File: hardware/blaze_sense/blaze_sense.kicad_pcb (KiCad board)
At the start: 2 copper layers, 70 x 70 mm, 2 parts, among them J2 Conn_01x30_Pin, J3 Conn_01x30_Socket

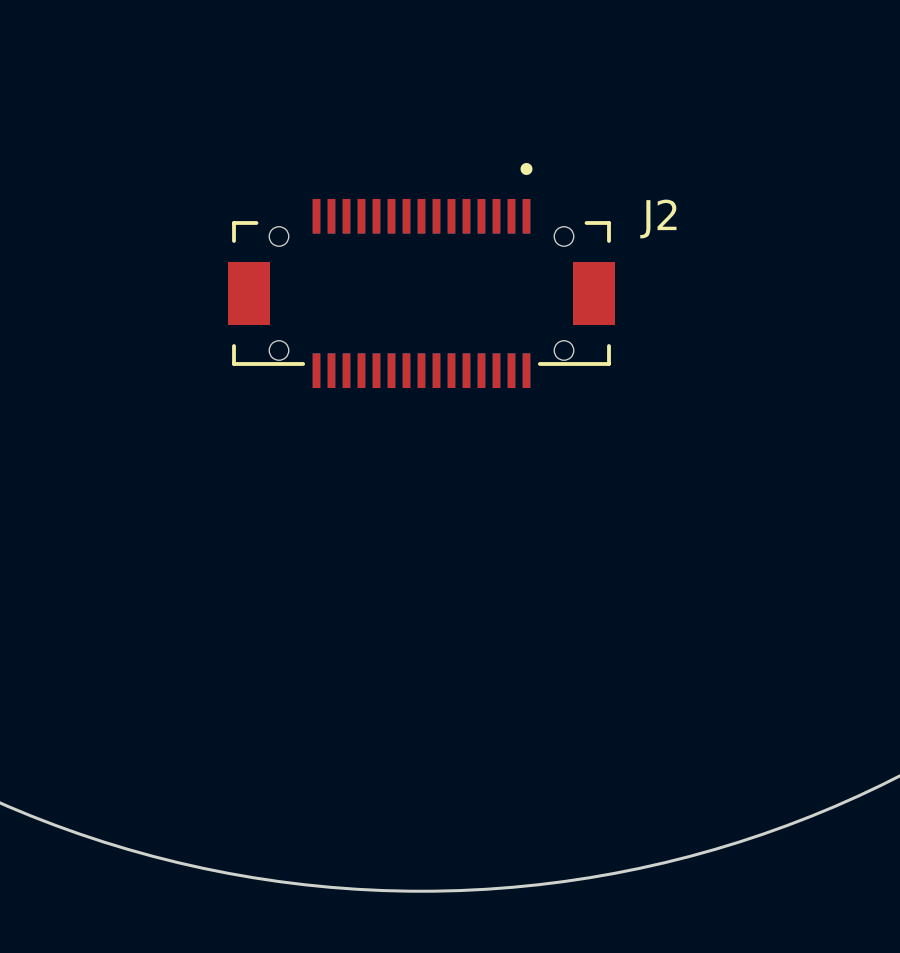
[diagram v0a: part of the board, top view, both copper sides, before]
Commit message: Brought in template PCB
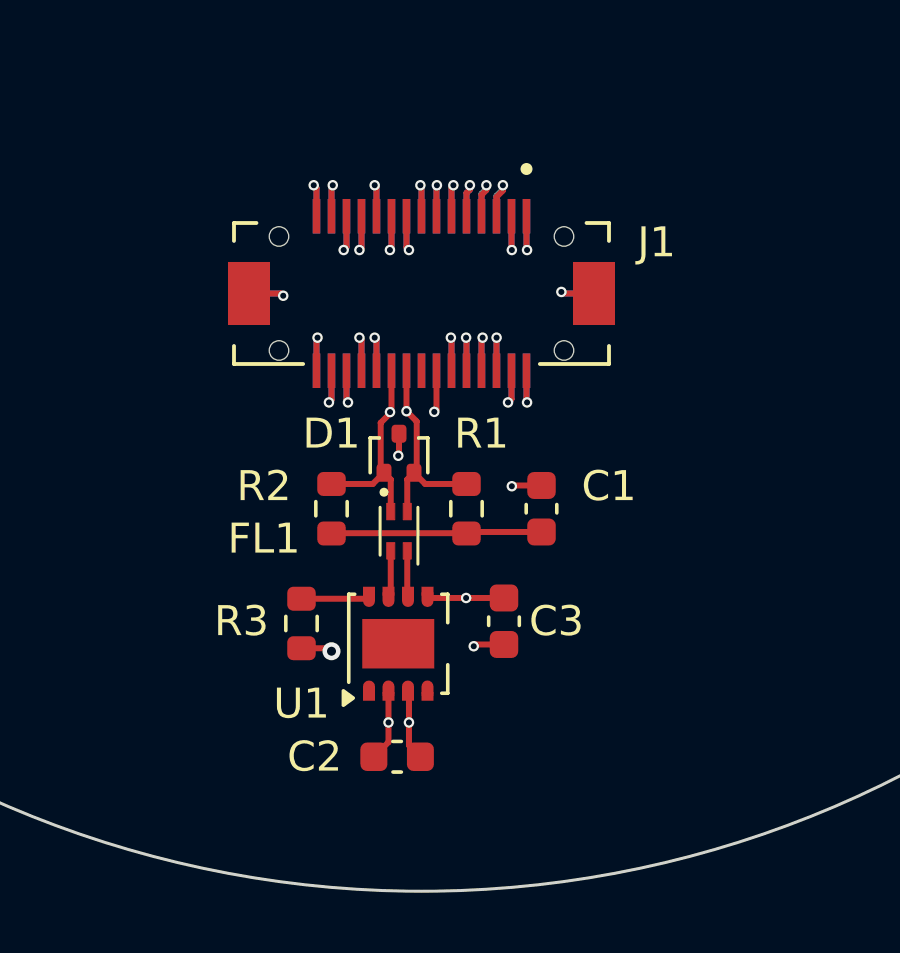
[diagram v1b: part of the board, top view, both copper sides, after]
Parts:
- added C1: 4.7nF, Capacitor_SMD:C_0603_1608Metric, F.Cu at (152.5, 127.8)
- added C2: 0.1uF, Capacitor_SMD:C_0603_1608Metric, F.Cu at (147.7, 136.0)
- added C3: 0.1uF, Capacitor_SMD:C_0603_1608Metric, F.Cu at (151.2, 131.5)
- added D1: ESDCAN03-2BM3Y, Package_TO_SOT_SMD:SOT-416, F.Cu at (147.8, 125.9)
- added FL1: Choke, Inductor_SMD:L_CommonModeChoke_Coilcraft_0603USB, F.Cu at (147.8, 128.5)
- added R1: 60, Resistor_SMD:R_0603_1608Metric, F.Cu at (150.0, 127.8)
- added R2: 60, Resistor_SMD:R_0603_1608Metric, F.Cu at (145.5, 127.8)
- added R3: 10K, Resistor_SMD:R_0603_1608Metric, F.Cu at (144.5, 131.6)
- added U1: TCAN1044VDDFR, Package_SON:Texas_S-PVSON-N8, F.Cu at (147.7, 132.2)
- J1: renamed from J2; value Conn_01x30_Pin -> FrontInterconnect
- J2: renamed from J3; value Conn_01x30_Socket -> RearInterconnect
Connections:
- J1 pad 1: Net-(J2-Pin_1) -> GND
- J1 pad 10: Net-(J2-Pin_10) -> +3V3
- J1 pad 11: +5V -> /PPS
- J1 pad 12: +3V3 -> GND
- J1 pad 13: /PPS -> GND
- J1 pad 14: GND -> Net-(J1-Pin_14)
- J1 pad 15: GND -> Net-(J1-Pin_15)
- J1 pad 16: Net-(J2-Pin_16) -> +3V3
- J1 pad 18: +3V3 -> Net-(J1-Pin_18)
- J1 pad 19: Net-(J2-Pin_19) -> GND
- J1 pad 2: Net-(J2-Pin_2) -> GND
- J1 pad 20: Net-(J2-Pin_20) -> GND
- J1 pad 21: GND -> /CANH
- J1 pad 22: GND -> /CANL
- J1 pad 23: /CANL -> Net-(J1-Pin_23)
- J1 pad 24: /CANH -> Net-(J1-Pin_24)
- J1 pad 25: Net-(J2-Pin_25) -> +5V
- J1 pad 26: Net-(J2-Pin_26) -> +5V
- J1 pad 27: +5V -> +3V3
- J1 pad 28: +5V -> +3V3
- J1 pad 29: +3V3 -> Net-(J1-Pin_29)
- J1 pad 3: GND -> /TX_RADIO
- J1 pad 30: +3V3 -> Net-(J1-Pin_30)
- J1 pad 4: GND -> /RX_RADIO
- J1 pad 5: /TX_RADIO -> Net-(J1-Pin_5)
- J1 pad 6: /RX_RADIO -> /ARM
- J1 pad 8: /ARM -> Net-(J1-Pin_8)
- J1 pad 9: Net-(J2-Pin_9) -> +5V
- J1 pad S1: (no net) -> GND
- J1 pad S2: (no net) -> GND
- J2 pad 1: +3V3 -> Net-(J1-Pin_30)
- J2 pad 10: GND -> /CANH
- J2 pad 11: Net-(J2-Pin_20) -> GND
- J2 pad 12: Net-(J2-Pin_19) -> GND
- J2 pad 13: +3V3 -> Net-(J1-Pin_18)
- J2 pad 15: Net-(J2-Pin_16) -> +3V3
- J2 pad 16: GND -> Net-(J1-Pin_15)
- J2 pad 17: GND -> Net-(J1-Pin_14)
- J2 pad 18: /PPS -> GND
- J2 pad 19: +3V3 -> GND
- J2 pad 2: +3V3 -> Net-(J1-Pin_29)
- J2 pad 20: +5V -> /PPS
- J2 pad 21: Net-(J2-Pin_10) -> +3V3
- J2 pad 22: Net-(J2-Pin_9) -> +5V
- J2 pad 23: /ARM -> Net-(J1-Pin_8)
- J2 pad 25: /RX_RADIO -> /ARM
- J2 pad 26: /TX_RADIO -> Net-(J1-Pin_5)
- J2 pad 27: GND -> /RX_RADIO
- J2 pad 28: GND -> /TX_RADIO
- J2 pad 29: Net-(J2-Pin_2) -> GND
- J2 pad 3: +5V -> +3V3
- J2 pad 30: Net-(J2-Pin_1) -> GND
- J2 pad 4: +5V -> +3V3
- J2 pad 5: Net-(J2-Pin_26) -> +5V
- J2 pad 6: Net-(J2-Pin_25) -> +5V
- J2 pad 7: /CANH -> Net-(J1-Pin_24)
- J2 pad 8: /CANL -> Net-(J1-Pin_23)
- J2 pad 9: GND -> /CANL
- J2 pad S1: (no net) -> GND
- J2 pad S2: (no net) -> GND
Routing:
- net +5V: track 0.00 -> 26.6 mm, vias 0 -> 4
- net GND: track 0.00 -> 23.2 mm, vias 0 -> 12
- net +3V3: track 0.00 -> 12.6 mm, vias 0 -> 6
- net Net-(C1-Pad1): track 0.00 -> 7.28 mm
- net /CANH: track 0.00 -> 6.94 mm, vias 0 -> 1
- net /CANL: track 0.00 -> 6.90 mm, vias 0 -> 1
- net /CAN_STB: track 0.00 -> 2.27 mm
- net /TX_RADIO: track 0.00 -> 2.24 mm, vias 0 -> 1
- net Net-(J1-Pin_29): track 0.00 -> 2.21 mm, vias 0 -> 1
- net /RX_RADIO: track 0.00 -> 2.20 mm, vias 0 -> 1
- net Net-(J1-Pin_17): track 0.00 -> 2.18 mm, vias 0 -> 1
- net Net-(J1-Pin_5): track 0.00 -> 2.16 mm, vias 0 -> 1
- net Net-(J1-Pin_18): track 0.00 -> 2.15 mm, vias 0 -> 1
- net Net-(J1-Pin_15): track 0.00 -> 2.14 mm, vias 0 -> 1
- net Net-(J1-Pin_30): track 0.00 -> 2.13 mm, vias 0 -> 1
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- added copper zone on In1.Cu, net +3V3
- added copper zone on In2.Cu, net GND
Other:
- copper layers 2 -> 4

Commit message: draft for julian to look over
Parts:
- added C1: 0.1uF, Capacitor_SMD:C_0603_1608Metric, F.Cu at (119.8, 103.9)
- added C10: 0.1uF, Capacitor_SMD:C_0603_1608Metric, F.Cu at (64.6, 82.8)
- added C11: 1uF, Capacitor_SMD:C_0603_1608Metric, F.Cu at (64.6, 85.3)
- added C12: 0.1uF, Capacitor_SMD:C_0603_1608Metric, F.Cu at (68.6, 60.2)
- added C13: 10nF, Capacitor_SMD:C_0603_1608Metric, F.Cu at (133.0, 88.2)
- added C14: 0.1uF, Capacitor_SMD:C_0603_1608Metric, F.Cu at (119.0, 96.9)
- added C15: 0.1uF, Capacitor_SMD:C_0603_1608Metric, F.Cu at (119.0, 94.8)
- added C16: 1uF, Capacitor_SMD:C_0603_1608Metric, F.Cu at (129.4, 99.3)
- added C17: 0.1uF, Capacitor_SMD:C_0603_1608Metric, F.Cu at (129.4, 101.3)
- added C18: 10uF, Capacitor_SMD:C_0603_1608Metric, F.Cu at (138.4, 85.3)
- added C19: 0.1uF, Capacitor_SMD:C_0603_1608Metric, F.Cu at (140.4, 85.3)
- added C2: 1uF, Capacitor_SMD:C_0603_1608Metric, F.Cu at (64.6, 62.8)
- added C20: 470nF, Capacitor_SMD:C_0603_1608Metric, F.Cu at (135.8, 88.2)
- added C21: 12.5pF, Capacitor_SMD:C_0603_1608Metric, F.Cu at (162.8, 112.5)
- added C22: 12.5pF, Capacitor_SMD:C_0603_1608Metric, F.Cu at (162.8, 108.9)
- added C23: 18pF, Capacitor_SMD:C_0603_1608Metric, F.Cu at (162.8, 104.5)
- added C24: 1uF, Capacitor_SMD:C_0603_1608Metric, F.Cu at (134.2, 102.3)
- added C25: 0.1uF, Capacitor_SMD:C_0603_1608Metric, F.Cu at (134.2, 100.5)
- added C26: 0.1uF, Capacitor_SMD:C_0603_1608Metric, F.Cu at (123.8, 103.9)
- added C27: 18pF, Capacitor_SMD:C_0603_1608Metric, F.Cu at (162.8, 100.7)
- added C28: 10uF, Capacitor_SMD:C_0603_1608Metric, F.Cu at (150.9, 98.2)
- added C29: 0.1uF, Capacitor_SMD:C_0603_1608Metric, F.Cu at (153.0, 98.3)
- added C3: 0.1uF, Capacitor_SMD:C_0603_1608Metric, F.Cu at (64.6, 65.3)
- added C30: 4.7nF, Capacitor_SMD:C_0603_1608Metric, F.Cu at (135.4, 126.3)
- added C31: 0.1uF, Capacitor_SMD:C_0603_1608Metric, F.Cu at (146.6, 115.5)
- added C32: 0.1uF, Capacitor_SMD:C_0603_1608Metric, F.Cu at (137.4, 115.5)
- added C33: 2.2uF, Capacitor_SMD:C_0603_1608Metric, F.Cu at (144.6, 97.8)
- added C34: 2.2uF, Capacitor_SMD:C_0603_1608Metric, F.Cu at (154.1, 114.3)
- added C35: 0.1uF, Capacitor_SMD:C_0603_1608Metric, F.Cu at (76.6, 62.8)
- added C36: 0.1uF, Capacitor_SMD:C_0603_1608Metric, F.Cu at (76.6, 65.3)
- added C37: 0.1uF, Capacitor_SMD:C_0603_1608Metric, F.Cu at (76.6, 67.8)
- added C38: 0.1uF, Capacitor_SMD:C_0603_1608Metric, F.Cu at (36.7, 64.8)
- added C39: 0.1uF, Capacitor_SMD:C_0603_1608Metric, F.Cu at (76.6, 72.8)
- added C4: 0.1uF, Capacitor_SMD:C_0603_1608Metric, F.Cu at (64.6, 67.8)
- added C40: 1uF, Capacitor_SMD:C_0603_1608Metric, F.Cu at (76.6, 75.3)
- added C5: 0.1uF, Capacitor_SMD:C_0603_1608Metric, F.Cu at (64.6, 70.3)
- added C6: 4.7uF, Capacitor_SMD:C_0603_1608Metric, F.Cu at (64.6, 72.8)
- added C7: 0.1uF, Capacitor_SMD:C_0603_1608Metric, F.Cu at (64.6, 75.3)
- added C8: 0.1uF, Capacitor_SMD:C_0603_1608Metric, F.Cu at (64.6, 77.8)
- added C9: 1uF, Capacitor_SMD:C_0603_1608Metric, F.Cu at (64.6, 80.3)
- added D1: D_Schottky, Diode_SMD:D_0603_1608Metric, F.Cu at (119.8, 106.3)
- added D2: ESDCAN03-2BM3Y, Package_TO_SOT_SMD:SOT-416, F.Cu at (142.3, 125.8)
- added FL1: Choke, Inductor_SMD:L_CommonModeChoke_Coilcraft_0603USB, F.Cu at (140.2, 121.4)
- added J2: Conn_01x30_Pin, BlazeLibrary:HRS_DF17_1.0H_-30DP-0.5V_57_, F.Cu at (173.3, 108.5)
- added J3: Conn_01x30_Socket, BlazeLibrary:HRS_DF17_1.0H_-30DP-0.5V_57_, F.Cu at (173.4, 100.3)
- added L1: L_Small, BlazeLibrary:SENSOR-XY-F-RM3100, F.Cu at (142.8, 82.8)
- added L2: L_Small, BlazeLibrary:SENSOR-XY-F-RM3100, F.Cu at (153.7, 85.3)
- added L3: L_Small, BlazeLibrary:SENSOR-Z-F-RM3100, F.Cu at (158.6, 94.9)
- added P1: TC2030-CTX, BlazeLibrary:TC2030-IDC-FP, F.Cu at (133.7, 108.0)
- added R10: 60, Resistor_SMD:R_0603_1608Metric, F.Cu at (138.3, 125.2)
- added R11: 60, Resistor_SMD:R_0603_1608Metric, F.Cu at (138.3, 127.3)
- added R12: 10K, Resistor_SMD:R_0603_1608Metric, F.Cu at (141.0, 130.6)
- added R2: 10k, Resistor_SMD:R_0603_1608Metric, F.Cu at (135.8, 84.5)
- added R3: 121, Resistor_SMD:R_0603_1608Metric, F.Cu at (148.3, 87.0)
- added R4: 121, Resistor_SMD:R_0603_1608Metric, F.Cu at (145.6, 87.0)
- added R5: 121, Resistor_SMD:R_0603_1608Metric, F.Cu at (154.8, 89.4)
- added R6: 121, Resistor_SMD:R_0603_1608Metric, F.Cu at (150.8, 89.4)
- added R7: 121, Resistor_SMD:R_0603_1608Metric, F.Cu at (153.1, 95.4)
- added R8: 121, Resistor_SMD:R_0603_1608Metric, F.Cu at (153.1, 93.0)
- added R9: 33k, Resistor_SMD:R_0603_1608Metric, F.Cu at (142.5, 88.2)
- added SW1: SW_SPST, Button_Switch_SMD:SW_SPST_B3U-1000P, F.Cu at (125.0, 108.0)
- added SW2: SW_SPDT, Button_Switch_SMD:Nidec_Copal_CAS-120A, F.Cu at (162.1, 124.5)
- added U1: ADXL375, BlazeLibrary:ADXL375BCCZ-RL, F.Cu at (132.0, 95.6)
- added U2: BMI088, BlazeLibrary:BMI088, F.Cu at (125.5, 94.9)
- added U3: A3G4250D, BlazeLibrary:A3G4250D, F.Cu at (139.5, 92.4)
- added U4: ADXL345, BlazeLibrary:ADXL345, F.Cu at (139.2, 99.1)
- added U5: MS5611-01BA, Package_LGA:LGA-8_3x5mm_P1.25mm, F.Cu at (124.7, 100.5)
- added U6: RM3100, BlazeLibrary:RM3100-13156, F.Cu at (146.6, 92.0)
- added U8: TCAN1044VDDFR, Package_SON:Texas_VSON-HR-8_1.5x2mm_P0.5mm, F.Cu at (142.0, 115.2)
- added U9: STM32H523RET6, BlazeLibrary:LQFP64_STM, F.Cu at (147.4, 107.0)
- added Y1: ABM3-8.000MHZ-B4Y-T, Crystal:Crystal_SMD_3215-2Pin_3.2x1.5mm, F.Cu at (159.4, 104.2)
- added Y2: ABS07-32.768KHZ-T, Crystal:Crystal_SMD_3215-2Pin_3.2x1.5mm, F.Cu at (159.3, 109.5)
- moved R3 0.07 mm to (144.5, 131.5)
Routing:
- net /SCK: track 0.00 -> 84.7 mm
- net /ARM: track 2.12 -> 72.3 mm, vias 1 -> 2
- net /PPS: track 2.12 -> 66.8 mm, vias 1 -> 2
- net /CANH: track 6.94 -> 69.4 mm, vias 1 -> 2
- net /CANL: track 6.90 -> 69.3 mm
- net /MOSI: track 0.00 -> 57.3 mm, vias 0 -> 3
- net /MISO: track 0.00 -> 50.8 mm, vias 0 -> 3
- net /TX_RADIO: track 2.24 -> 49.2 mm, vias 1 -> 2
- net /RESET: track 0.00 -> 43.0 mm
- net /RX_RADIO: track 2.20 -> 41.2 mm, vias 1 -> 2
- net /CANRX: track 0.00 -> 36.4 mm
- net Net-(J2-Pin_7): track 0.00 -> 36.1 mm
- net Net-(J2-Pin_8): track 0.00 -> 30.7 mm
- net /CANTX: track 0.00 -> 30.5 mm, vias 0 -> 2
- net Net-(J2-Pin_5): track 0.00 -> 29.2 mm
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
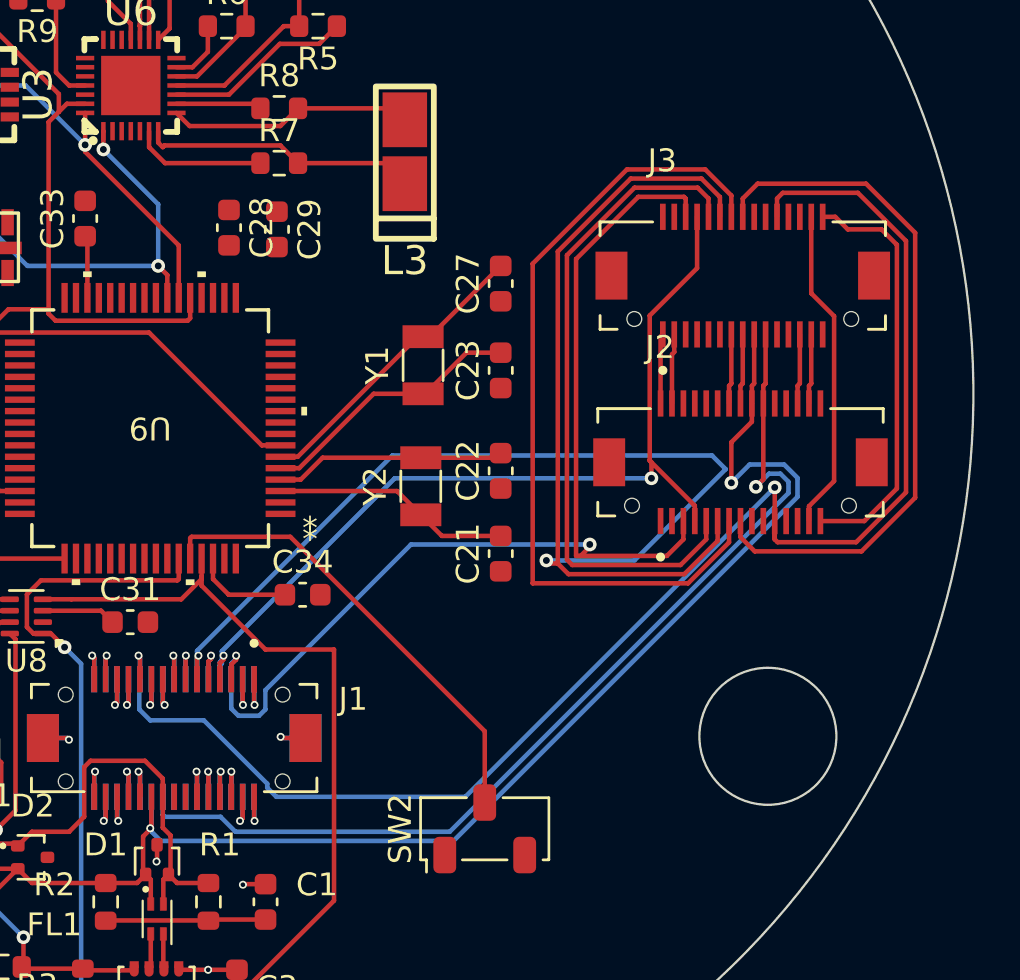
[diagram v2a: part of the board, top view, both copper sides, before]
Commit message: Removed extra interconnect footprints
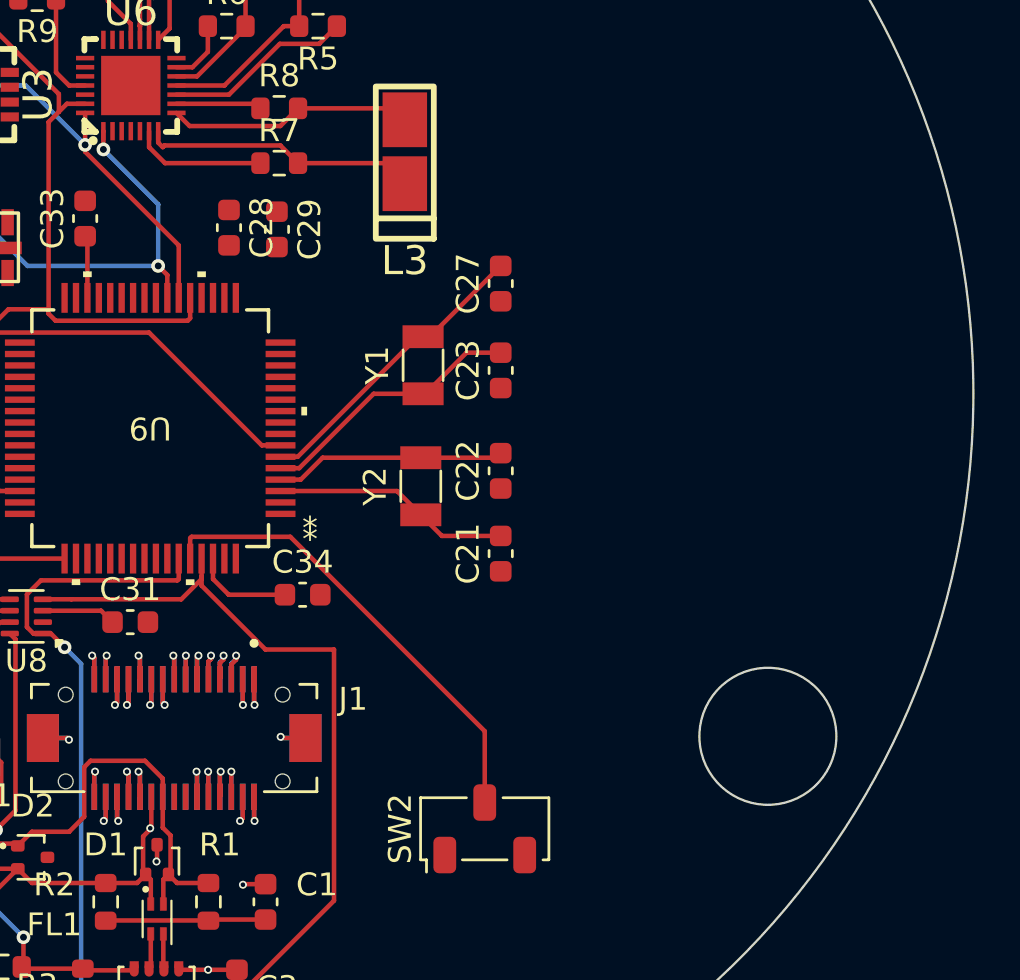
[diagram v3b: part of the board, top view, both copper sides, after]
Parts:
- removed the J2 at (173.3, 108.5)
- removed J3: Conn_01x30_Socket, BlazeLibrary:HRS_DF17_1.0H_-30DP-0.5V_57_
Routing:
- net /ARM: track 72.3 -> 2.12 mm, vias 2 -> 1
- net /PPS: track 66.8 -> 2.12 mm, vias 2 -> 1
- net /CANH: track 69.4 -> 21.9 mm, vias 2 -> 1
- net /TX_RADIO: track 49.2 -> 2.24 mm, vias 2 -> 1
- net /CANL: track 69.3 -> 25.5 mm, vias 1 -> 0
- net /RX_RADIO: track 41.2 -> 2.20 mm, vias 2 -> 1
- net Net-(J2-Pin_7): track 36.1 -> 0.00 mm
- net Net-(J2-Pin_8): track 30.7 -> 0.00 mm
- net Net-(J2-Pin_5): track 29.2 -> 0.00 mm
- net Net-(J2-Pin_15): track 18.4 -> 0.00 mm
- net Net-(J2-Pin_14): track 14.2 -> 0.00 mm
- net Net-(J2-Pin_30): track 3.07 -> 0.00 mm
- net Net-(J2-Pin_29): track 3.07 -> 0.00 mm
- net Net-(J2-Pin_24): track 3.07 -> 0.00 mm
- net Net-(J2-Pin_23): track 3.07 -> 0.00 mm
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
